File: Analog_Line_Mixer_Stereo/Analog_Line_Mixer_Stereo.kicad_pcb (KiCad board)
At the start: 2 copper layers, 0 parts

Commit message: mostly finalized component placement, starting routing
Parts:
- added C1: 1uF, Capacitors_SMD:C_1206, B.Cu at (134.0, 130.2)
- added C10: 10uF, Capacitors_SMD:C_1206, B.Cu at (153.7, 158.1)
- added C11: 4.7nF, Capacitors_SMD:C_1206, B.Cu at (150.5, 150.5)
- added C2: 1uF, Capacitors_SMD:C_1206, B.Cu at (134.0, 133.3)
- added C3: 1000uF, Capacitors_SMD:C_1206, B.Cu at (125.1, 147.3)
- added C4: 27pF, Capacitors_SMD:C_1206, B.Cu at (127.6, 118.7)
- added C5: 27pF, Capacitors_SMD:C_1206, B.Cu at (116.8, 133.3)
- added C6: 47uF, Capacitors_SMD:C_1206, B.Cu at (150.5, 144.1)
- added C7: 47uF, Capacitors_SMD:C_1206, B.Cu at (123.8, 157.5)
- added C8: 47uF, Capacitors_SMD:C_1206, B.Cu at (116.8, 158.1)
- added C9: 22uF, 10V, Capacitors_SMD:C_1206, B.Cu at (137.2, 160.0)
- added CON1: BARREL_JACK, CUI-INC:Barrel_Jack_2.1x5.5mm_CUI_INC, F.Cu at (151.1, 166.4)
- added D1: 1N4001, Diodes_SMD:SOD-323, B.Cu at (147.3, 163.8)
- added D2: 1N4001, Diodes_SMD:SOD-323, B.Cu at (130.2, 159.4)
- added D3: POWER_TEST, LEDs:LED_0603, B.Cu at (137.8, 166.4)
- added D4: D_Schottky, Diodes_SMD:SOD-123, B.Cu at (127.0, 157.5)
- added J1: IN-1, CUI-INC:SJ1-353XNG-5Pin, F.Cu at (122.6, 110.5)
- added J2: IN-2, CUI-INC:SJ1-353XNG-5Pin, F.Cu at (122.6, 124.5)
- added J3: IN-3, CUI-INC:SJ1-353XNG-5Pin, F.Cu at (122.6, 139.7)
- added J4: IN-4, CUI-INC:SJ1-353XNG-5Pin, F.Cu at (122.6, 152.4)
- added J5: OUT, CUI-INC:SJ1-353XNG-5Pin, F.Cu at (122.6, 163.8)
- added L1: 10uH, Resistors_SMD:R_0805, B.Cu at (134.0, 165.7)
- added P1: USB_B, Connect:USB_Micro-B, B.Cu at (128.9, 172.7)
- added R1: 10K, Resistors_SMD:R_1206, F.Cu at (132.7, 123.2)
- added R10: 100k, Resistors_SMD:R_1206, B.Cu at (127.6, 115.6)
- added R11: 18k, Resistors_SMD:R_1206, B.Cu at (136.5, 142.2)
- added R12: 100k, Resistors_SMD:R_1206, B.Cu at (120.0, 133.3)
- added R13: 22k, Resistors_SMD:R_1206, B.Cu at (153.7, 144.1)
- added R14: 100, Resistors_SMD:R_1206, B.Cu at (115.6, 149.2)
- added R15: 100, Resistors_SMD:R_1206, B.Cu at (120.0, 154.9)
- added R16: 24k9, Resistors_SMD:R_1206, B.Cu at (150.5, 158.1)
- added R17: 3k48, Resistors_SMD:R_1206, B.Cu at (142.2, 171.4)
- added R18: 30k1, Resistors_SMD:R_1206, B.Cu at (145.4, 171.4)
- added R2: 10K, Resistors_SMD:R_1206, F.Cu at (132.7, 109.2)
- added R3: 10K, Resistors_SMD:R_1206, F.Cu at (132.7, 127.0)
- added R4: 10K, Resistors_SMD:R_1206, F.Cu at (132.7, 142.2)
- added R5: 10K, Resistors_SMD:R_1206, F.Cu at (132.7, 138.4)
- added R6: 10K, Resistors_SMD:R_1206, F.Cu at (132.7, 154.9)
- added R7: 10K, Resistors_SMD:R_1206, F.Cu at (132.7, 151.1)
- added R8: 10K, Resistors_SMD:R_1206, F.Cu at (132.7, 113.0)
- added R9: 2k, Resistors_SMD:R_1206, B.Cu at (125.7, 167.6)
- added RV1: 100K, Taiwan_Alpha:TA-Dual-Pot-pin-RV122F, F.Cu at (143.5, 111.8)
- added RV2: 100K, Taiwan_Alpha:TA-Dual-Pot-pin-RV122F, F.Cu at (143.5, 125.7)
- added RV3: 100K, Taiwan_Alpha:TA-Dual-Pot-pin-RV122F, F.Cu at (143.5, 139.7)
- added RV4: 100K, Taiwan_Alpha:TA-Dual-Pot-pin-RV122F, F.Cu at (143.5, 153.7)
- added SW1: POWER_TEST, Grayhill:Grayhill-38F-M6-SPST, F.Cu at (119.4, 170.2)
- added SW2: Power Selector, Grayhill:Grayhill-47B-switches-SPDT-M6, F.Cu at (139.7, 162.6)
- added U1: RC4560, texas:TI-LM2698-MUA08A, B.Cu at (125.1, 132.7)
- added U2: LM2698, texas:TI-LM2698-MUA08A, B.Cu at (137.8, 170.8)
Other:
- board outline added: 41.9 x 73.7 mm

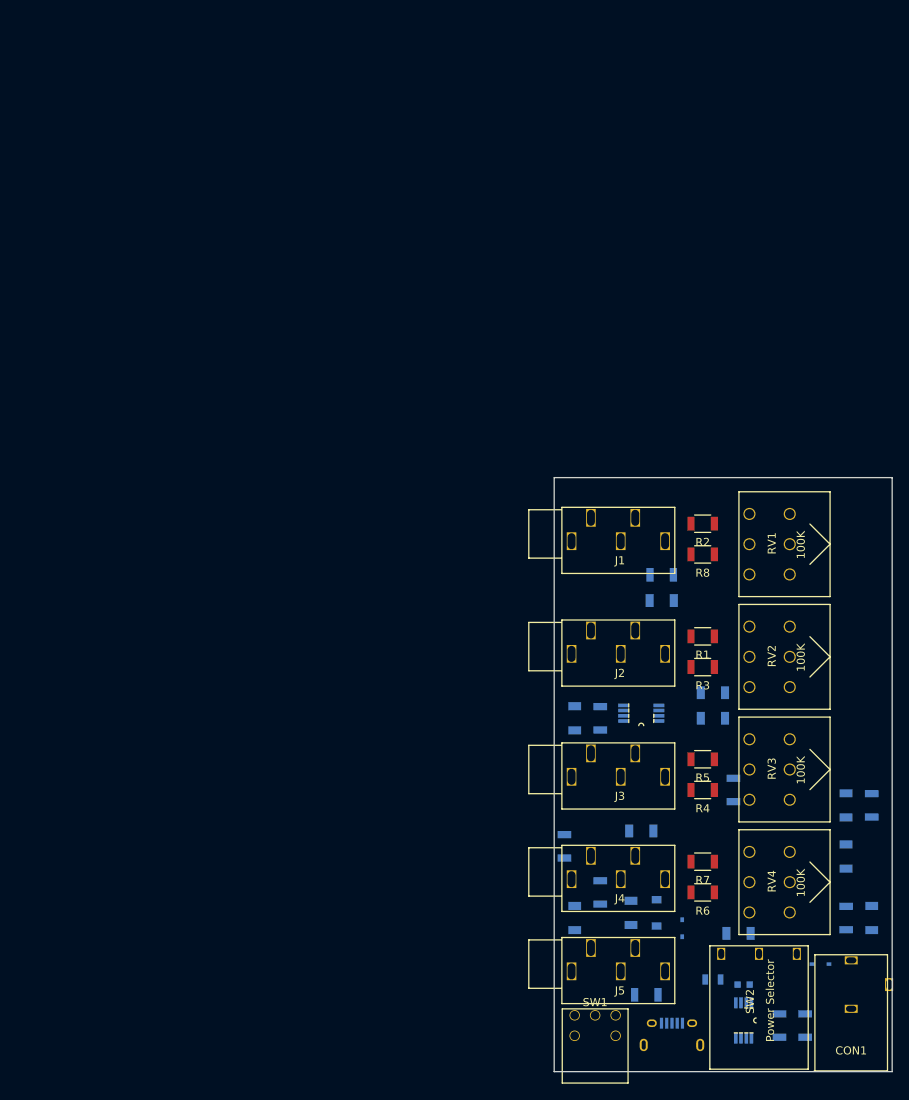
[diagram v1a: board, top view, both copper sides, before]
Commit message: routing mostly finished, need to check TSSOP package and other packages for soldermask specs
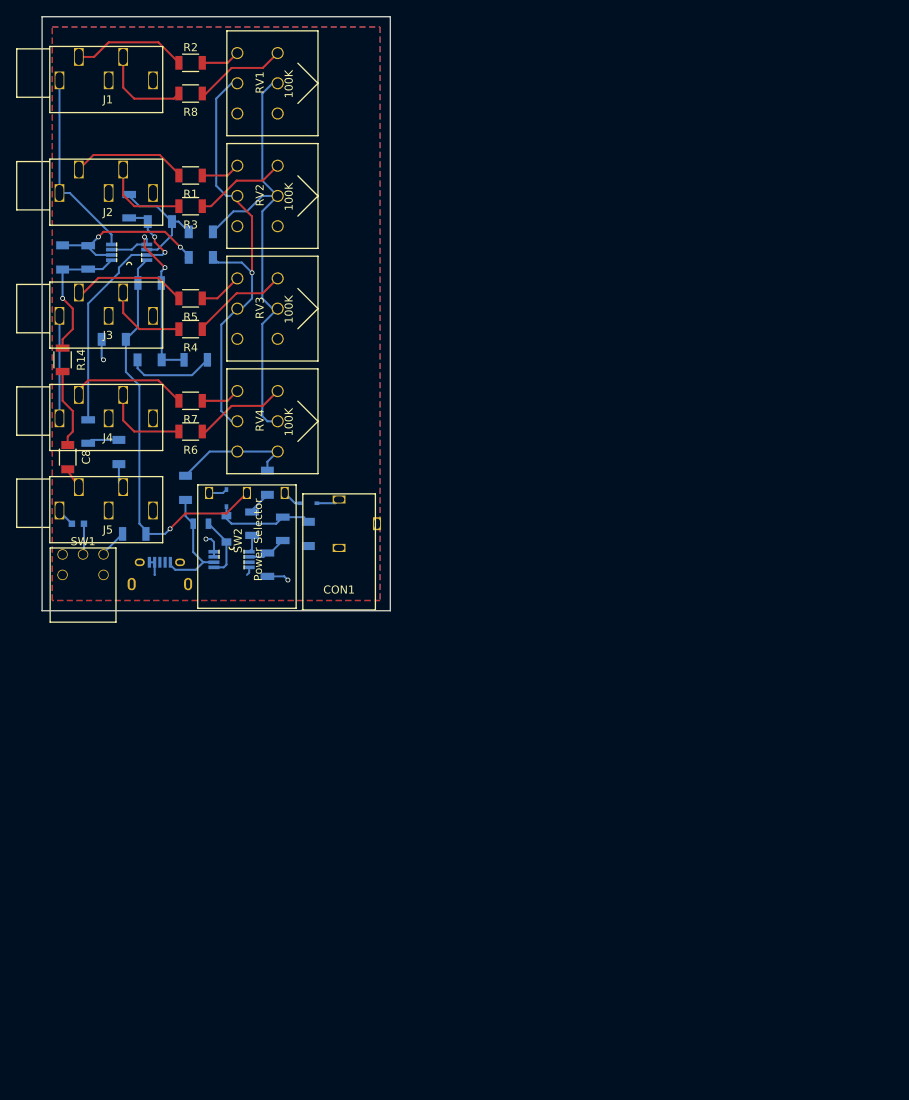
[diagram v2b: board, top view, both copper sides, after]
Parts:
- C8, R14: moved to F.Cu
- moved C6 102.5 mm to (64.1, 88.9), turned to 180 degrees
- moved D3 100.4 mm to (55.2, 109.2)
- moved R13 100.4 mm to (69.8, 88.9), turned to 0 degrees
- moved R11 95.9 mm to (64.1, 79.4), turned to 0 degrees
- moved C3 89.4 mm to (59.7, 86.4)
- moved R18 89.4 mm to (80.6, 109.9)
- moved R16 88.4 mm to (76.8, 109.2)
- moved C9 88.1 mm to (68.6, 104.8), turned to 90 degrees
- moved R14 86.7 mm to (53.3, 88.9)
- moved J4 85.4 mm to (59.1, 95.2)
- moved J5 85.4 mm to (59.1, 106.7)
- moved C1 85.4 mm to (70.5, 73.0)
- moved C2 85.4 mm to (70.5, 76.2)
- moved CON1 85.4 mm to (87.6, 109.2)
- moved D1 85.4 mm to (83.8, 106.7)
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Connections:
- CON1 pad 2: Net-(CON1-Pad2) -> GND
- CON1 pad 3: Net-(CON1-Pad2) -> GND
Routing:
- net GND: track 0.00 -> 77.8 mm, vias 0 -> 3
- net /RSUM: track 0.00 -> 58.0 mm
- net /LSUM: track 0.00 -> 54.8 mm, vias 0 -> 1
- net VCC: track 0.00 -> 50.7 mm, vias 0 -> 1
- net Net-(C4-Pad1): track 0.00 -> 34.1 mm, vias 0 -> 2
- net /+B: track 0.00 -> 24.9 mm, vias 0 -> 2
- net Net-(C2-Pad1): track 0.00 -> 21.7 mm, vias 0 -> 2
- net Net-(C5-Pad1): track 0.00 -> 17.4 mm, vias 0 -> 1
- net /Power_Regulator/Vin: track 0.00 -> 15.2 mm
- net Net-(C1-Pad1): track 0.00 -> 15.0 mm
- net Net-(J4-Pad2): track 0.00 -> 14.6 mm
- net Net-(J2-Pad2): track 0.00 -> 14.3 mm
- net Net-(J3-Pad2): track 0.00 -> 14.2 mm
- net Net-(J1-Pad2): track 0.00 -> 14.2 mm
- net +12V: track 0.00 -> 12.5 mm
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- added copper zone on B.Cu, net GND
- added copper zone on F.Cu, net GND
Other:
- board size 41.9 x 73.7 mm -> 43.2 x 73.7 mm

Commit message: adding footprints and dimensions
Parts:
- added REF**: MountingHole_3mm, Mounting_Holes:MountingHole_3mm, F.Cu at (88.9, 52.1)
- added REF**: MountingHole_3mm, Mounting_Holes:MountingHole_3mm, F.Cu at (88.9, 94.6)
- added REF**: MountingHole_3mm, Mounting_Holes:MountingHole_3mm, F.Cu at (69.2, 61.6)
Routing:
- net Net-(D4-Pad2): track 7.69 -> 13.8 mm, vias 0 -> 2
- net GND: track 77.8 -> 80.1 mm, vias 3 -> 4
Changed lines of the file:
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@@
     (area 47.379999 40.33 105.79 121.705001)
     (thickness 1.6)
-    (drawings 6)
-    (tracks 252)
+    (drawings 9)
+    (tracks 260)
     (zones 0)
-    (modules 49)
+    (modules 52)
     (nets 41)
   )
@@
       (net 6 GND))
   )
+  (module Mounting_Holes:MountingHole_3mm (layer F.Cu)
+    (at 88.9 52.07)
+    (descr "Mounting hole, Befestigungsbohrung, 3mm, No Annular, Kein Restring,")
+    (tags "Mounting hole, Befestigungsbohrung, 3mm, No Annular, Kein Restring,")
+    (fp_text reference REF** (at 0 -4.0005) (layer F.SilkS)
+      (effects (font (size 1 1) (thickness 0.15)))
+    )
+    (fp_text value MountingHole_3mm (at 1.00076 5.00126) (layer F.Fab)
+      (effects (font (size 1 1) (thickness 0.15)))
+    )
+    (fp_circle (center 0 0) (end 3 0) (layer Cmts.User) (width 0.381))
+    (pad 1 thru_hole circle (at 0 0) (size 3 3) (drill 3) (layers))
+  )
+  (module Mounting_Holes:MountingHole_3mm (layer F.Cu)
+    (at 88.9 94.615)
+    (descr "Mounting hole, Befestigungsbohrung, 3mm, No Annular, Kein Restring,")
+    (tags "Mounting hole, Befestigungsbohrung, 3mm, No Annular, Kein Restring,")
+    (fp_text reference REF** (at 0 -4.0005) (layer F.SilkS)
+      (effects (font (size 1 1) (thickness 0.15)))
+    )
+    (fp_text value MountingHole_3mm (at 1.00076 5.00126) (layer F.Fab)
+      (effects (font (size 1 1) (thickness 0.15)))
+    )
+    (fp_circle (center 0 0) (end 3 0) (layer Cmts.User) (width 0.381))
+    (pad 1 thru_hole circle (at 0 0) (size 3 3) (drill 3) (layers))
+  )
+  (module Mounting_Holes:MountingHole_3mm (layer F.Cu)
+    (at 69.215 61.595)
+    (descr "Mounting hole, Befestigungsbohrung, 3mm, No Annular, Kein Restring,")
+    (tags "Mounting hole, Befestigungsbohrung, 3mm, No Annular, Kein Restring,")
+    (fp_text reference REF** (at 0 -4.0005) (layer F.SilkS)
+      (effects (font (size 1 1) (thickness 0.15)))
+    )
+    (fp_text value MountingHole_3mm (at 1.00076 5.00126) (layer F.Fab)
+      (effects (font (size 1 1) (thickness 0.15)))
+    )
+    (fp_circle (center 0 0) (end 3 0) (layer Cmts.User) (width 0.381))
+    (pad 1 thru_hole circle (at 0 0) (size 3 3) (drill 3) (layers))
+  )
+  (dimension 13.97 (width 0.3) (layer Cmts.User)
+    (gr_text "13.970 mm" (at 43.1 54.61 90) (layer Cmts.User)
+      (effects (font (size 1.5 1.5) (thickness 0.3)))
+    )
+    (feature1 (pts (xy 69.215 47.625) (xy 41.75 47.625)))
+    (feature2 (pts (xy 69.215 61.595) (xy 41.75 61.595)))
+    (crossbar (pts (xy 44.45 61.595) (xy 44.45 47.625)))
+    (arrow1a (pts (xy 44.45 47.625) (xy 45.036421 48.751504)))
+    (arrow1b (pts (xy 44.45 47.625) (xy 43.863579 48.751504)))
+    (arrow2a (pts (xy 44.45 61.595) (xy 45.036421 60.468496)))
+    (arrow2b (pts (xy 44.45 61.595) (xy 43.863579 60.468496)))
+  )
+  (dimension 24.765 (width 0.3) (layer Cmts.User)
+    (gr_text "24.765 mm" (at 81.5975 35.48) (layer Cmts.User)
+      (effects (font (size 1.5 1.5) (thickness 0.3)))
+    )
+    (feature1 (pts (xy 93.98 61.595) (xy 93.98 34.13)))
+    (feature2 (pts (xy 69.215 61.595) (xy 69.215 34.13)))
+    (crossbar (pts (xy 69.215 36.83) (xy 93.98 36.83)))
+    (arrow1a (pts (xy 93.98 36.83) (xy 92.853496 37.416421)))
+    (arrow1b (pts (xy 93.98 36.83) (xy 92.853496 36.243579)))
+    (arrow2a (pts (xy 69.215 36.83) (xy 70.341504 37.416421)))
+    (arrow2b (pts (xy 69.215 36.83) (xy 70.341504 36.243579)))
+  )
+  (dimension 42.545 (width 0.3) (layer Cmts.User)
+    (gr_text "42.545 mm" (at 104.855 73.3425 270) (layer Cmts.User)
+      (effects (font (size 1.5 1.5) (thickness 0.3)))
+    )
+    (feature1 (pts (xy 88.9 94.615) (xy 106.205 94.615)))
+    (feature2 (pts (xy 88.9 52.07) (xy 106.205 52.07)))
+    (crossbar (pts (xy 103.505 52.07) (xy 103.505 94.615)))
+    (arrow1a (pts (xy 103.505 94.615) (xy 102.918579 93.488496)))
+    (arrow1b (pts (xy 103.505 94.615) (xy 104.091421 93.488496)))
+    (arrow2a (pts (xy 103.505 52.07) (xy 102.918579 53.196504)))
+    (arrow2b (pts (xy 103.505 52.07) (xy 104.091421 53.196504)))
+  )
   (dimension 73.66 (width 0.3) (layer Cmts.User)
     (gr_text "73.660 mm" (at 99.14 83.185 270) (layer Cmts.User)
@@
   (via (at 66.675 109.855) (size 0.6) (drill 0.4) (layers F.Cu B.Cu) (net 5))
   (segment (start 66.04 110.49) (end 66.675 109.855) (width 0.25) (layer B.Cu) (net 5))
+  (segment (start 76.47686 114.6302) (end 74.5998 114.6302) (width 0.25) (layer B.Cu) (net 6))
+  (via (at 74.295 114.935) (size 0.6) (drill 0.4) (layers F.Cu B.Cu) (net 6))
+  (segment (start 74.5998 114.6302) (end 74.295 114.935) (width 0.25) (layer B.Cu) (net 6))
   (segment (start 76.47686 114.6302) (end 76.47686 115.29314) (width 0.25) (layer B.Cu) (net 6))
   (segment (start 76.47686 115.29314) (end 76.2 115.57) (width 0.25) (layer B.Cu) (net 6))
@@
   (segment (start 55.9943 109.22) (end 55.9943 112.9157) (width 0.25) (layer B.Cu) (net 20))
   (segment (start 55.9943 112.9157) (end 55.88 113.03) (width 0.25) (layer B.Cu) (net 20))
+  (segment (start 72.11314 114.6302) (end 72.0598 114.6302) (width 0.25) (layer B.Cu) (net 21))
+  (segment (start 72.0598 114.6302) (end 71.12 115.57) (width 0.25) (layer B.Cu) (net 21))
+  (via (at 71.12 115.57) (size 0.6) (drill 0.4) (layers F.Cu B.Cu) (net 21))
+  (segment (start 71.12 115.57) (end 73.66 113.03) (width 0.25) (layer F.Cu) (net 21))
+  (segment (start 73.66 113.03) (end 73.66 109.855) (width 0.25) (layer F.Cu) (net 21))
+  (via (at 73.66 109.855) (size 0.6) (drill 0.4) (layers F.Cu B.Cu) (net 21))
+  (segment (start 73.66 109.855) (end 73.025 109.22) (width 0.25) (layer B.Cu) (net 21))
+  (segment (start 73.025 109.22) (end 71.435 109.22) (width 0.25) (layer B.Cu) (net 21))
   (segment (start 73.66 111.49) (end 73.66 111.445) (width 0.25) (layer B.Cu) (net 21))
   (segment (start 73.66 111.445) (end 71.435 109.22) (width 0.25) (layer B.Cu) (net 21))
-  (segment (start 72.11314 114.6302) (end 73.3298 114.6302) (width 0.25) (layer B.Cu) (net 21))
-  (segment (start 73.66 114.3) (end 73.66 111.49) (width 0.25) (layer B.Cu) (net 21))
-  (segment (start 73.3298 114.6302) (end 73.66 114.3) (width 0.25) (layer B.Cu) (net 21))
   (segment (start 55.355 51.34) (end 57.245 51.34) (width 0.25) (layer F.Cu) (net 22))
   (segment (start 65.225 49.53) (end 67.765 52.07) (width 0.25) (layer F.Cu) (net 22))

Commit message: creating gerbers
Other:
- board text added: "Analog Stereo Line Mixer With Apologies to Rolls"
- board text added: "Stephen Walker-Weinshenker"
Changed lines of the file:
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@@
     (links 93)
     (no_connects 0)
-    (area 47.379999 40.33 105.79 121.705001)
+    (area 36.450001 33.98 111.505 122.515)
     (thickness 1.6)
-    (drawings 9)
+    (drawings 17)
     (tracks 260)
     (zones 0)
@@
     (34 B.Paste user)
     (35 F.Paste user)
-    (36 B.SilkS user hide)
+    (36 B.SilkS user)
     (37 F.SilkS user)
     (38 B.Mask user)
@@
     (pad_drill 0.762)
     (pad_to_mask_clearance 0.2)
-    (aux_axis_origin 0 0)
+    (aux_axis_origin 50.8 120.015)
     (grid_origin 140.97 110.49)
     (visible_elements FFFEFF7F)
@@
       (plotinvisibletext false)
       (padsonsilk false)
-      (subtractmaskfromsilk false)
+      (subtractmaskfromsilk true)
       (outputformat 1)
       (mirror false)
       (drillshape 0)
       (scaleselection 1)
-      (outputdirectory ""))
+      (outputdirectory Gerbers/))
   )
   (net 0 "")
@@
     (pad 1 thru_hole circle (at 0 0) (size 3 3) (drill 3) (layers))
   )
+  (target plus (at 46.355 120.015) (size 5) (width 0.15) (layer Edge.Cuts))
+  (target plus (at 46.355 120.015) (size 5) (width 0.15) (layer Edge.Cuts))
+  (target plus (at 46.355 43.18) (size 5) (width 0.15) (layer Edge.Cuts))
+  (target plus (at 46.355 43.18) (size 5) (width 0.15) (layer Edge.Cuts))
+  (target plus (at 97.79 43.18) (size 5) (width 0.15) (layer Edge.Cuts))
+  (target plus (at 97.79 43.18) (size 5) (width 0.15) (layer Edge.Cuts))
+  (gr_text "Stephen Walker-Weinshenker" (at 88.9 73.025 90) (layer B.Cu)
+    (effects (font (size 1.5 1.5) (thickness 0.3)))
+  )
+  (gr_text "Analog Stereo Line Mixer\nWith Apologies to Rolls" (at 88.9 73.66 90) (layer F.Cu)
+    (effects (font (size 1.5 1.5) (thickness 0.3)))
+  )
   (dimension 13.97 (width 0.3) (layer Cmts.User)
